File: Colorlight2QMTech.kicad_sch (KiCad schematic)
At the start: 16 parts, among them CN1 1473005-4, J1 Conn_02x32_Odd_Even, J2 Conn_02x32_Odd_Even, J3 Connector_USB_C_Receptacle_US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, J4-GND1 Conn_01x01_Male, SW1 TS-1187A-B-A-B, U1 AMS1117-3.3

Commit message: tidy schematic and export
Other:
- moved on the sheet: C1, C2, C3, C4, C5, F1, FB1, J3, R1, U1

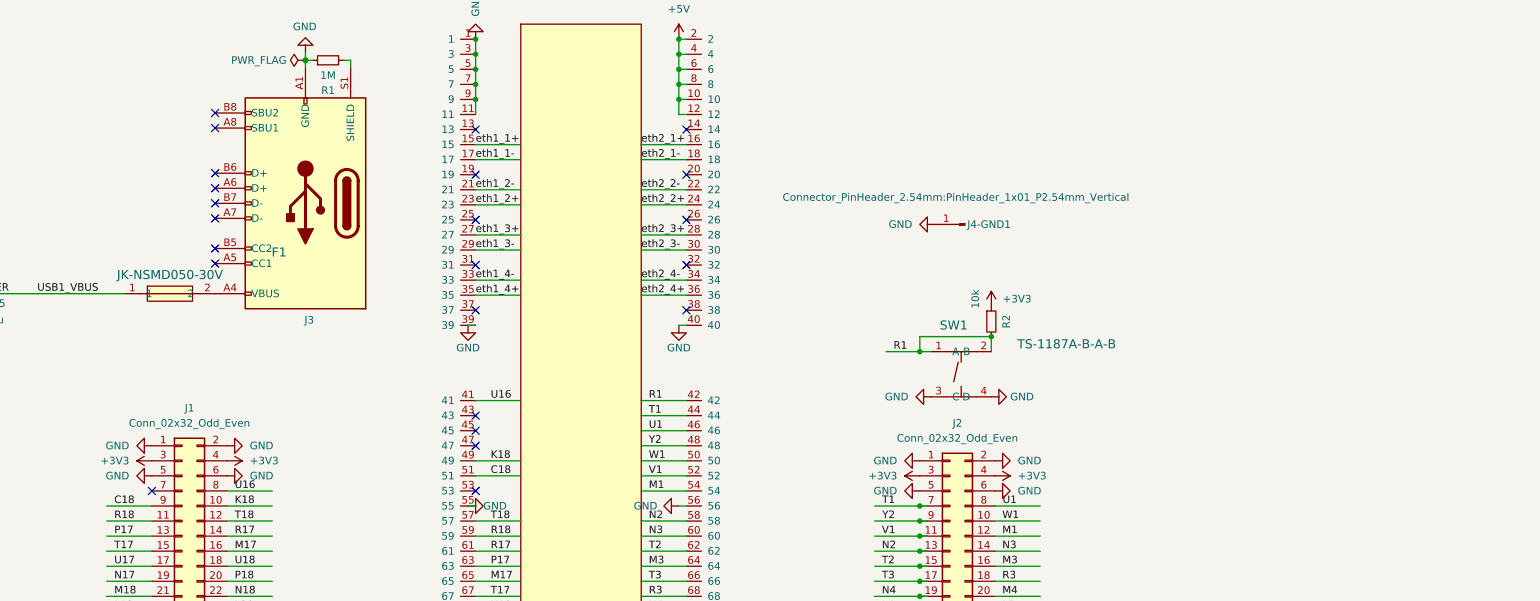
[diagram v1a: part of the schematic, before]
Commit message: New revision and first release: Fixed routing issues, better silk screen, break out ethernet signals.
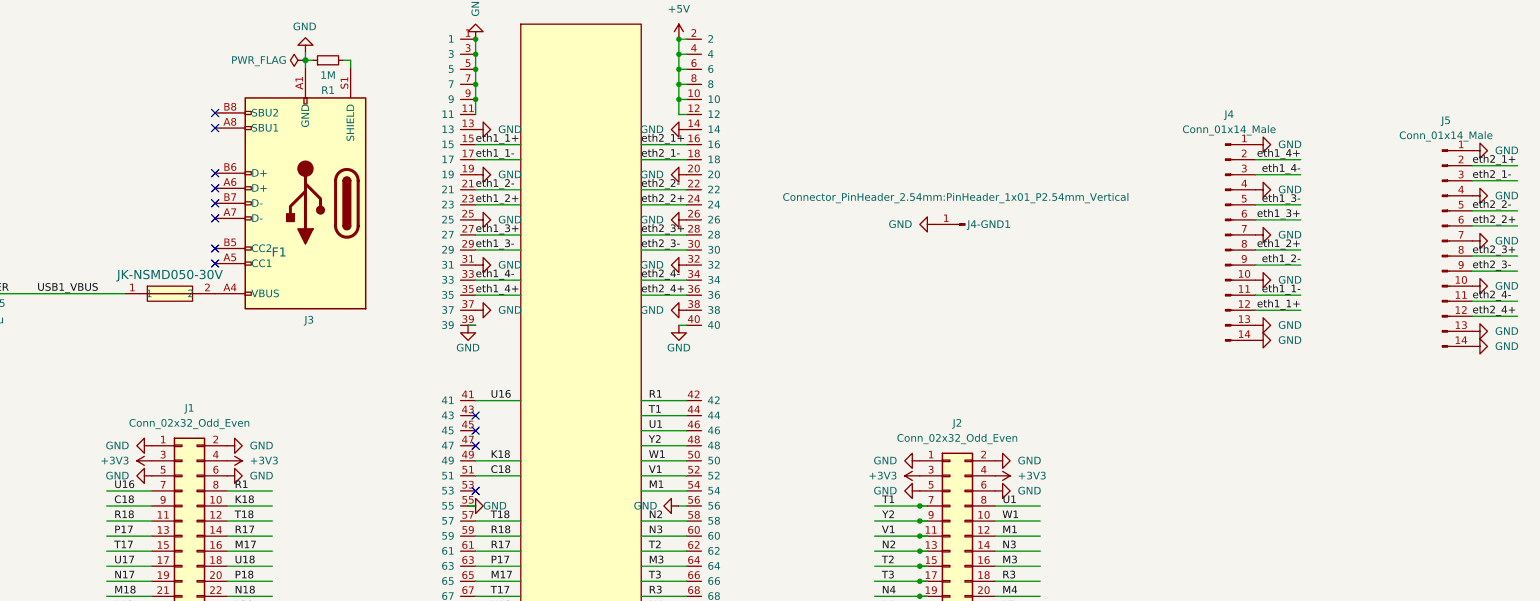
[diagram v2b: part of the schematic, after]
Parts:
- removed R2: 10k, Resistor_SMD:R_0603_1608Metric, symbol Device:R_Small
- removed SW1: TS-1187A-B-A-B, easyeda2kicad:SW-SMD_4P-L5.1-W5.1-P3.70-LS6.5-TL-2, symbol easyeda2kicad:TS-1187A-B-A-B
- added J4, J5: Conn_01x14_Male, symbol Connector:Conn_01x14_Male
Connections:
- net GND: now also CN1.13, CN1.14, CN1.19, CN1.20, CN1.25, CN1.26, CN1.31, CN1.32, CN1.37, CN1.38, J4.1 (Pin_1), J4.10 (Pin_10), J4.13 (Pin_13), J4.14 (Pin_14), J4.4 (Pin_4), J4.7 (Pin_7), J5.1 (Pin_1), J5.10 (Pin_10), J5.13 (Pin_13), J5.14 (Pin_14), J5.4 (Pin_4), J5.7 (Pin_7)
- net R1: now also J1.8 (Pin_8)
- net U16: now also J1.7 (Pin_7); no longer J1.8 (Pin_8)
- net eth1_1+: now also J4.12 (Pin_12)
- net eth1_1-: now also J4.11 (Pin_11)
- net eth1_2+: now also J4.8 (Pin_8)
- net eth1_2-: now also J4.9 (Pin_9)
- net eth1_3+: now also J4.6 (Pin_6)
- net eth1_3-: now also J4.5 (Pin_5)
- net eth1_4+: now also J4.2 (Pin_2)
- net eth1_4-: now also J4.3 (Pin_3)
- net eth2_1+: now also J5.2 (Pin_2)
- net eth2_1-: now also J5.3 (Pin_3)
- net eth2_2+: now also J5.6 (Pin_6)
- net eth2_2-: now also J5.5 (Pin_5)
- net eth2_3+: now also J5.8 (Pin_8)
- net eth2_3-: now also J5.9 (Pin_9)
- net eth2_4+: now also J5.12 (Pin_12)
- net eth2_4-: now also J5.11 (Pin_11)
- no-connect marks 65 -> 54

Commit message: beautify schematic and export
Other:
- company: (none) -> Hans Baier
- title: (none) -> Colorlight i5/i9 to QMTech Adapter Board
- moved on the sheet: C1, C2, C3, C4, C5, CN1, F1, FB1, J1, J2, J3, J4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

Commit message: make alternate version with an upright connector
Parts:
- CN1: value 1473005-4 -> (none); footprint easyeda2kicad:SO-DIMM-SMD_200P-P0.60_1473005-4 -> (none); LCSC Part C428482 -> C483268
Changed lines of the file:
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@@
       (effects (font (size 1.524 1.524)))
     )
-    (property "Value" "1473005-4" (id 1) (at 208.534 288.798 0)
+    (property "Value" "" (id 1) (at 208.534 288.798 0)
       (effects (font (size 1.524 1.524)))
     )
-    (property "Footprint" "easyeda2kicad:SO-DIMM-SMD_200P-P0.60_1473005-4" (id 2) (at 208.534 302.006 0)
+    (property "Footprint" "" (id 2) (at 208.534 302.006 0)
       (effects (font (size 1.524 1.524)) hide)
     )
@@
       (effects (font (size 0 0)) hide)
     )
-    (property "LCSC Part" "C428482" (id 5) (at 208.534 154.686 0)
+    (property "LCSC Part" "C483268" (id 5) (at 208.534 154.686 0)
       (effects (font (size 0 0)) hide)
     )
@@
     )
     (path "/bab3fc61-7ffc-43fd-b7e1-a49971a5fd5e"
-      (reference "CN1") (unit 1) (value "1473005-4") (footprint "easyeda2kicad:SO-DIMM-SMD_200P-P0.60_1473005-4")
+      (reference "CN1") (unit 1) (value "1473005-4") (footprint "easyeda2kicad:DIMM-SMD_DM-7D4-H2500-M")
     )
     (path "/39076acb-b2f1-4d8b-9854-ef54cb071b0d"

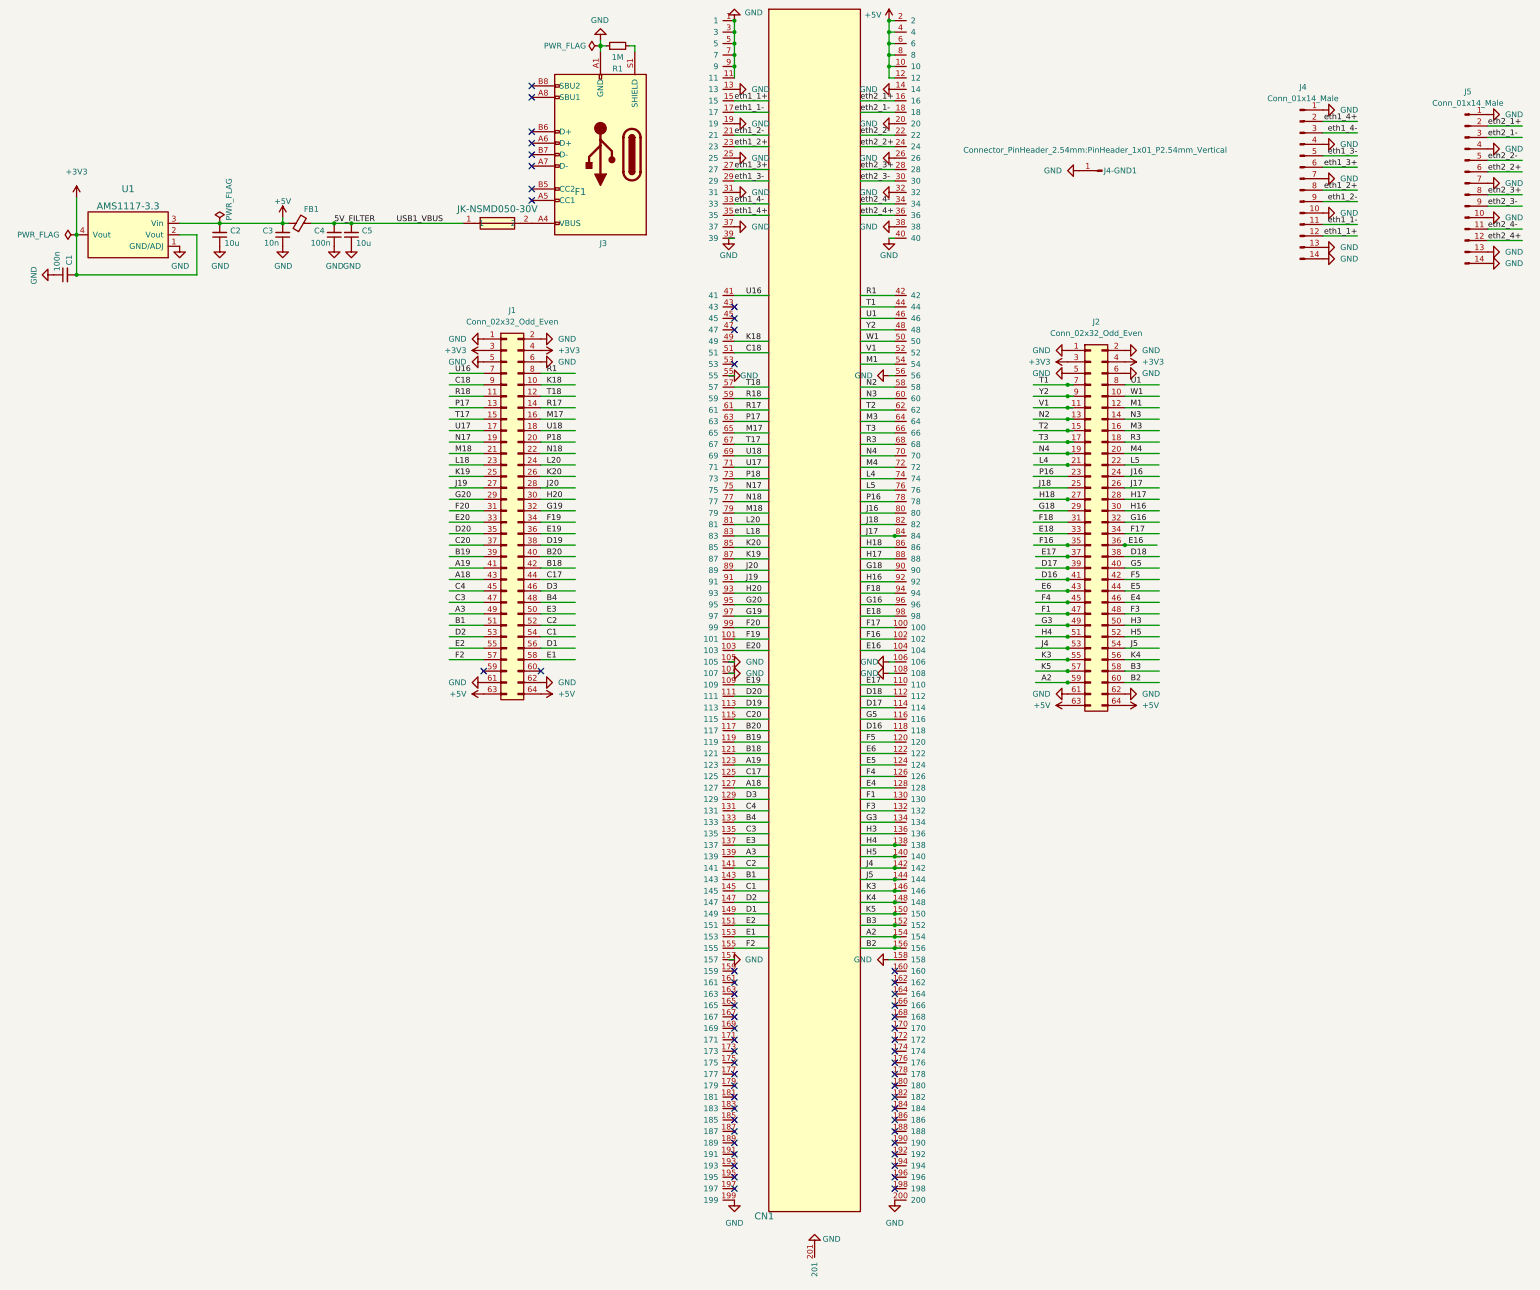
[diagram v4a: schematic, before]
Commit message: add upright variant with ethernet connectors
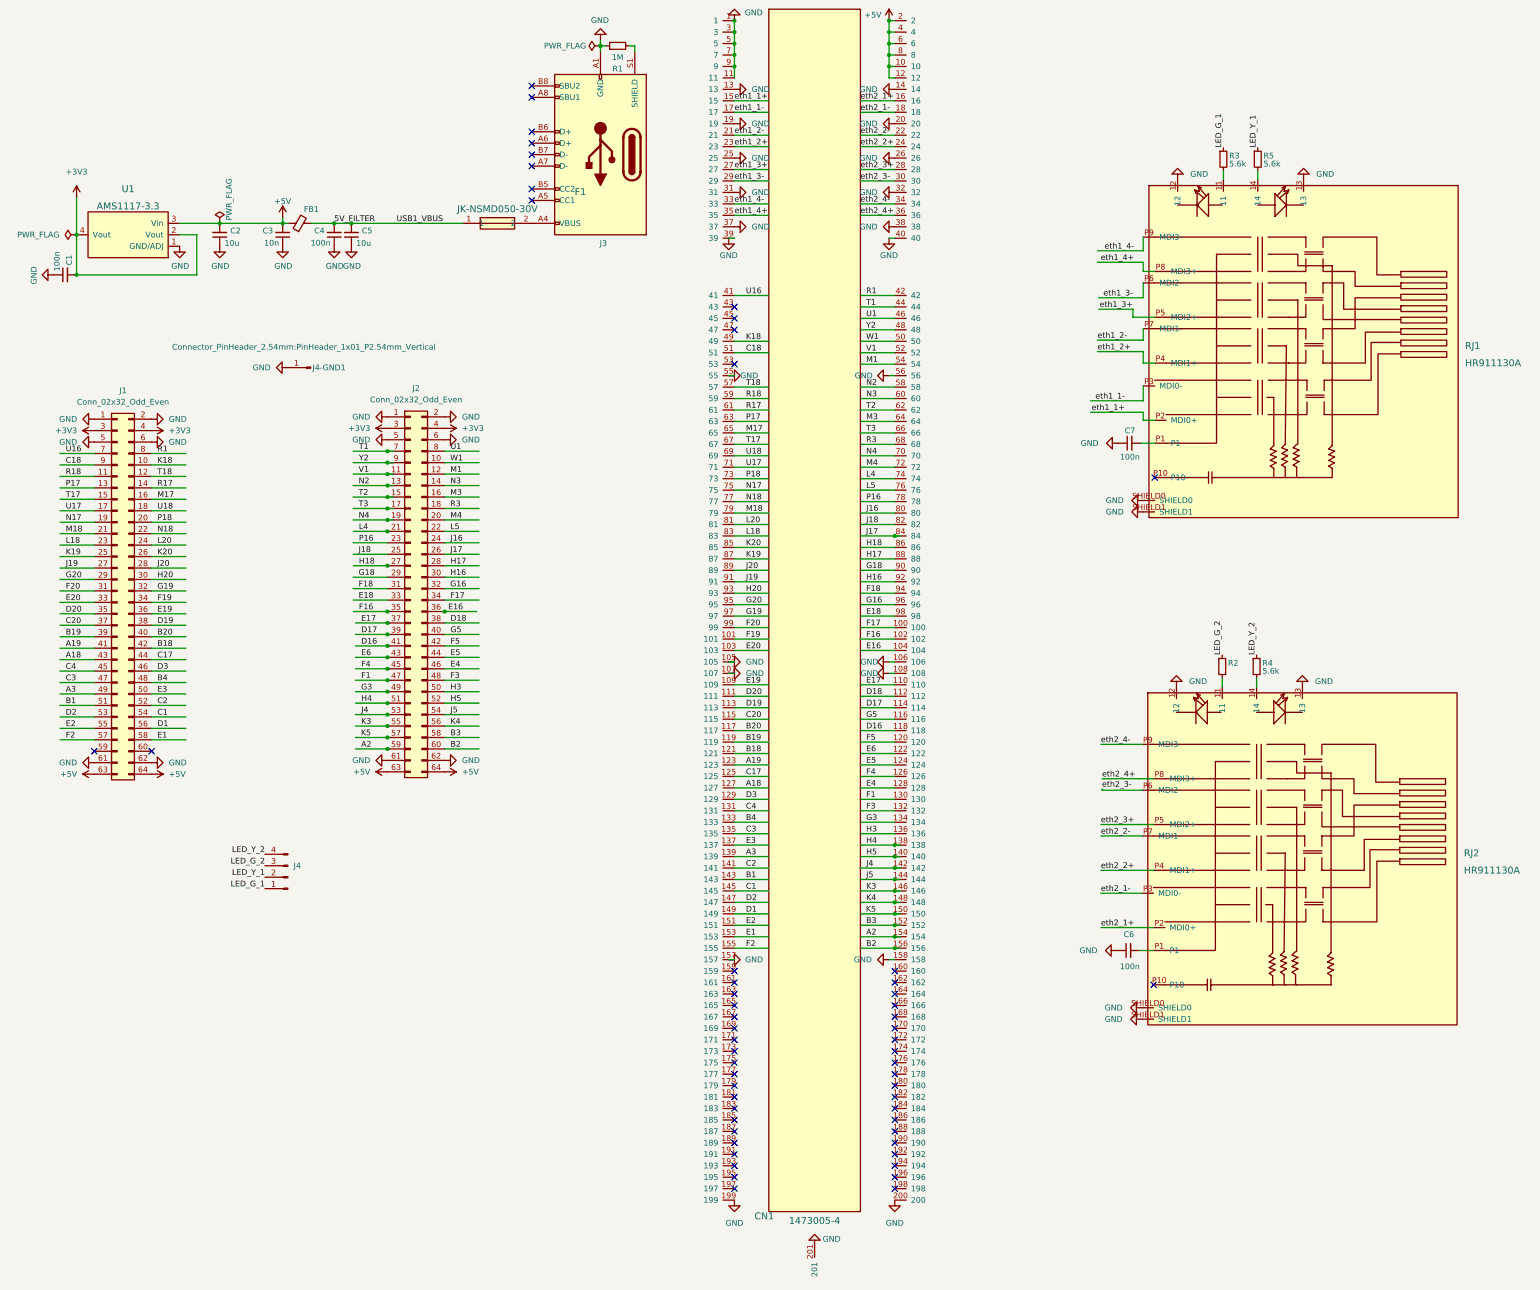
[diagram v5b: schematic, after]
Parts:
- removed J4, J5: Conn_01x14_Male, symbol Connector:Conn_01x14_Male
- added C6, C7: 100n, Capacitor_SMD:C_0603_1608Metric, symbol Device:C_Small
- added J4: (no value), symbol Connector:Conn_01x04_Male
- added R2: (no value), symbol jlcpcb-basic-resistor:R_0603_5.6k
- added R3, R4, R5: 5.6k, R_0603_1608Metric, symbol jlcpcb-basic-resistor:R_0603_5.6k
- added RJ1, RJ2: HR911130A, RJ45-TH_HR911130A, symbol easyeda2kicad:HR911130A
- CN1: value (none) -> 1473005-4; footprint (none) -> easyeda2kicad:DIMM-SMD_DM-7D4-H2500-M
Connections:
- net GND: now also C6.1, C7.1, RJ1.12, RJ1.13, RJ1.SHIELD0, RJ1.SHIELD1, RJ2.12, RJ2.13, RJ2.SHIELD0, RJ2.SHIELD1
- net eth1_1+: now also RJ1.P2 (MDI0+)
- net eth1_1-: now also RJ1.P3 (MDI0-)
- net eth1_2+: now also RJ1.P4 (MDI1+)
- net eth1_2-: now also RJ1.P7 (MDI1-)
- net eth1_3+: now also RJ1.P5 (MDI2+)
- net eth1_3-: now also RJ1.P6 (MDI2-)
- net eth1_4+: now also RJ1.P8 (MDI3+)
- net eth1_4-: now also RJ1.P9 (MDI3-)
- net eth2_1+: now also RJ2.P2 (MDI0+)
- net eth2_1-: now also RJ2.P3 (MDI0-)
- net eth2_2+: now also RJ2.P4 (MDI1+)
- net eth2_2-: now also RJ2.P7 (MDI1-)
- net eth2_3+: now also RJ2.P5 (MDI2+)
- net eth2_3-: now also RJ2.P6 (MDI2-)
- net eth2_4+: now also RJ2.P8 (MDI3+)
- net eth2_4-: now also RJ2.P9 (MDI3-)
- new net: R3.2, RJ1.11
- new net: R5.2, RJ1.14
- new net: C7.2, RJ1.P1
- new net: R2.2, RJ2.11
- new net: R4.2, RJ2.14
- new net: C6.2, RJ2.P1
- new net LED_G_1: J4.1 (Pin_1), R3.1
- new net LED_G_2: J4.3 (Pin_3), R2.1
- new net LED_Y_1: J4.2 (Pin_2), R5.1
- new net LED_Y_2: J4.4 (Pin_4), R4.1
- no-connect marks 54 -> 56
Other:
- moved on the sheet: J1, J2, J4-GND1

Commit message: add variant with horizontal SODIMM connector and ethernet
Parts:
- CN1: footprint easyeda2kicad:DIMM-SMD_DM-7D4-H2500-M -> easyeda2kicad:SO-DIMM-SMD_200P-P0.60_1473005-4
- J4: value (none) -> Conn_01x04_Male
- R2: value (none) -> 5.6k; footprint (none) -> R_0603_1608Metric
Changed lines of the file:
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@@
       (effects (font (size 1.27 1.27)) (justify right))
     )
-    (property "Value" "" (id 1) (at 92.964 212.5979 0)
+    (property "Value" "Conn_01x04_Male" (id 1) (at 92.964 212.5979 0)
       (effects (font (size 1.27 1.27)) (justify right))
     )
@@
       (effects (font (size 1.524 1.524)))
     )
-    (property "Footprint" "easyeda2kicad:DIMM-SMD_DM-7D4-H2500-M" (id 2) (at 208.534 302.006 0)
+    (property "Footprint" "easyeda2kicad:SO-DIMM-SMD_200P-P0.60_1473005-4" (id 2) (at 208.534 302.006 0)
       (effects (font (size 1.524 1.524)) hide)
     )
@@
       (effects (font (size 1.27 1.27)) (justify left))
     )
-    (property "Value" "" (id 1) (at 300.228 166.878 0)
-      (effects (font (size 1.27 1.27)) (justify left))
-    )
-    (property "Footprint" "" (id 2) (at 297.18 165.862 90)
+    (property "Value" "5.6k" (id 1) (at 300.228 166.878 0)
+      (effects (font (size 1.27 1.27)) (justify left))
+    )
+    (property "Footprint" "R_0603_1608Metric" (id 2) (at 297.18 165.862 90)
       (effects (font (size 1.27 1.27)) hide)
     )
@@
     )
     (path "/bab3fc61-7ffc-43fd-b7e1-a49971a5fd5e"
-      (reference "CN1") (unit 1) (value "1473005-4") (footprint "easyeda2kicad:DIMM-SMD_DM-7D4-H2500-M")
+      (reference "CN1") (unit 1) (value "1473005-4") (footprint "easyeda2kicad:SO-DIMM-SMD_200P-P0.60_1473005-4")
     )
     (path "/39076acb-b2f1-4d8b-9854-ef54cb071b0d"
